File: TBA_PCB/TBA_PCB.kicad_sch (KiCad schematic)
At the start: 0 parts

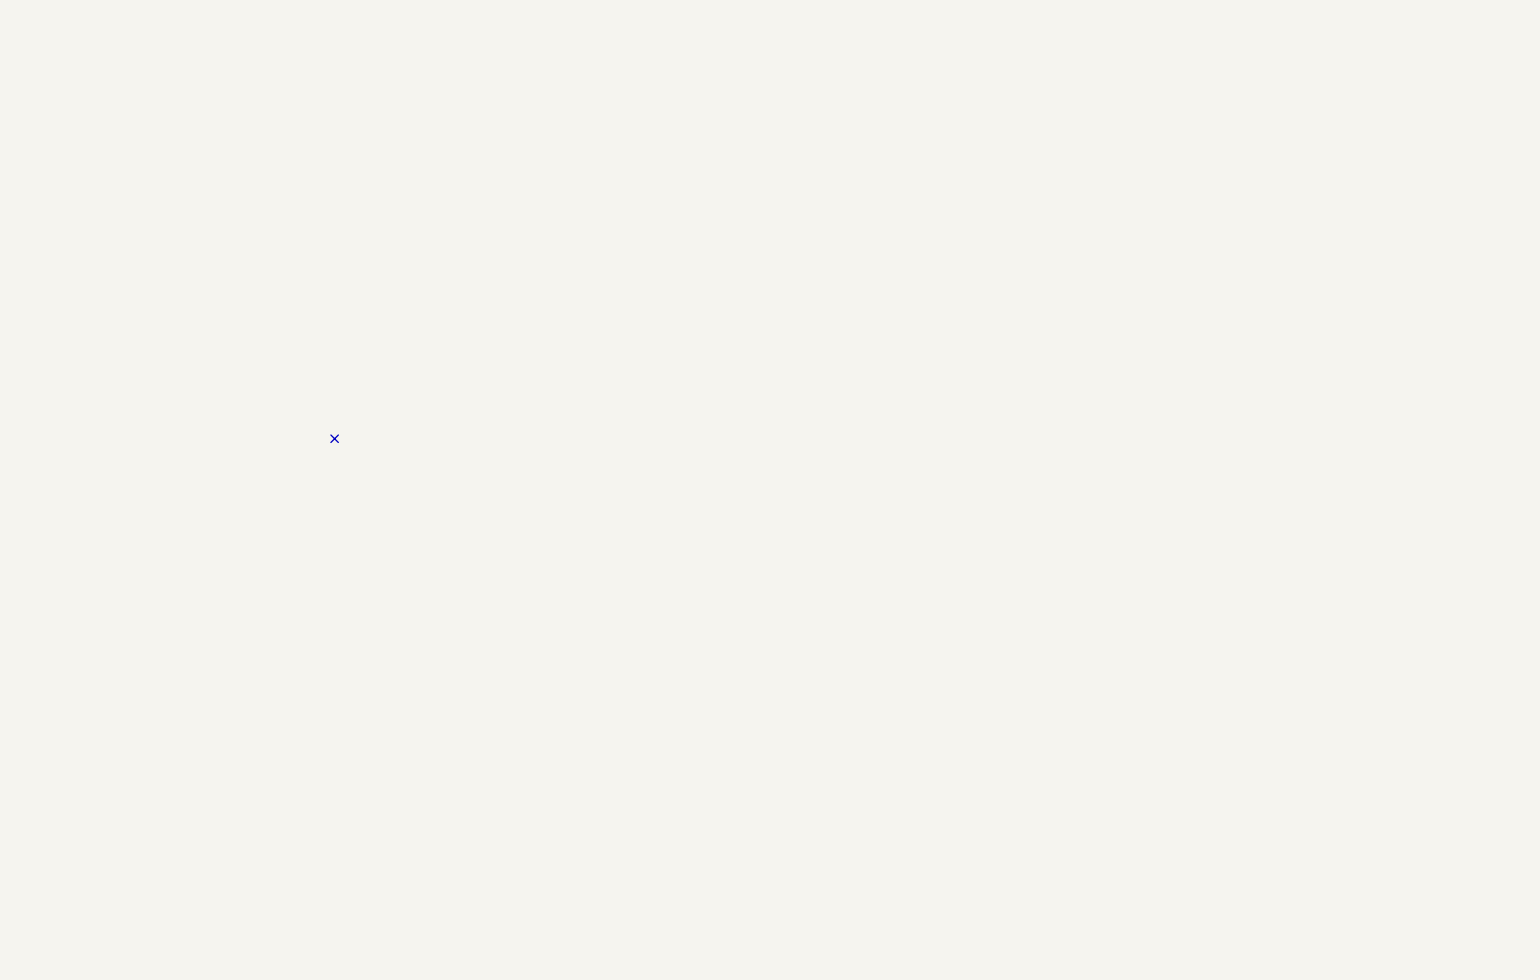
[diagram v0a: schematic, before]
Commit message: included practice threshold, updated PCB, gathered new data to plot
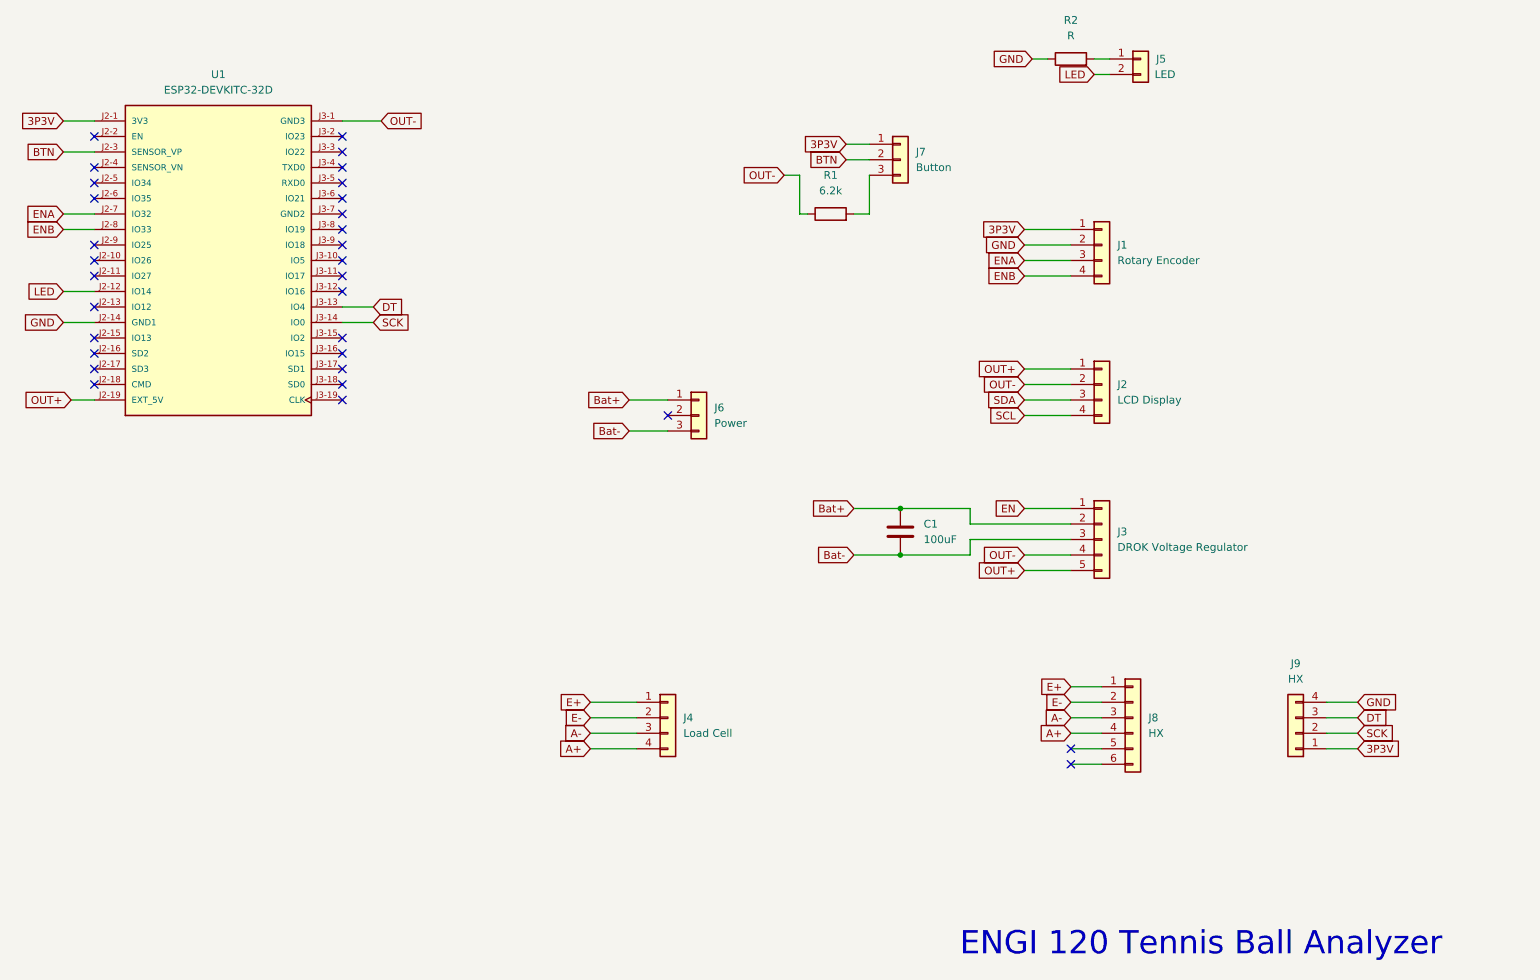
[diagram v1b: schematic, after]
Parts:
- added C1: 100uF, Capacitor_THT:CP_Radial_D4.0mm_P2.00mm, symbol Device:C
- added J1: Rotary Encoder, Connector_PinHeader_2.54mm:PinHeader_1x04_P2.54mm_Vertical, symbol Connector_Generic:Conn_01x04
- added J2: LCD Display, Connector_PinHeader_2.54mm:PinHeader_1x04_P2.54mm_Vertical, symbol Connector_Generic:Conn_01x04
- added J3: DROK Voltage Regulator, Connector_PinHeader_2.54mm:PinHeader_1x05_P2.54mm_Vertical, symbol Connector_Generic:Conn_01x05
- added J4: Load Cell, Connector_PinHeader_2.54mm:PinHeader_1x04_P2.54mm_Vertical, symbol Connector_Generic:Conn_01x04
- added J5: LED, Connector_PinHeader_2.54mm:PinHeader_1x02_P2.54mm_Vertical, symbol Connector_Generic:Conn_01x02
- added J6: Power, Connector_PinHeader_2.54mm:PinHeader_1x03_P2.54mm_Vertical, symbol Connector_Generic:Conn_01x03
- added J7: Button, Connector_PinHeader_2.54mm:PinHeader_1x03_P2.54mm_Vertical, symbol Connector_Generic:Conn_01x03
- added J8: HX, Connector_PinHeader_2.54mm:PinHeader_1x06_P2.54mm_Vertical, symbol Connector_Generic:Conn_01x06
- added J9: HX, Connector_PinHeader_2.54mm:PinHeader_1x04_P2.54mm_Vertical, symbol Connector_Generic:Conn_01x04
- added R1: 6.2k, Resistor_THT:R_Axial_DIN0204_L3.6mm_D1.6mm_P2.54mm_Vertical, symbol Device:R
- added R2: R, Resistor_THT:R_Axial_DIN0204_L3.6mm_D1.6mm_P2.54mm_Vertical, symbol Device:R
- added U1: ESP32-DEVKITC-32D, KiCad Footprints:MODULE_ESP32-DEVKITC-32D, symbol ESP32-DEVKITC-32D:ESP32-DEVKITC-32D
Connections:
- new net: J7.3 (Pin_3), R1.2
- new net: J5.1 (Pin_1), R2.2
- new net 3P3V: J1.1 (Pin_1), J7.1 (Pin_1), J9.1 (Pin_1), U1.J2-1 (3V3)
- new net A+: J4.4 (Pin_4), J8.4 (Pin_4)
- new net A-: J4.3 (Pin_3), J8.3 (Pin_3)
- new net BTN: J7.2 (Pin_2), U1.J2-3 (SENSOR_VP)
- new net Bat+: C1.1, J3.2 (Pin_2), J6.1 (Pin_1)
- new net Bat-: C1.2, J3.3 (Pin_3), J6.3 (Pin_3)
- new net DT: J9.3 (Pin_3), U1.J3-13 (IO4)
- new net E+: J4.1 (Pin_1), J8.1 (Pin_1)
- new net E-: J4.2 (Pin_2), J8.2 (Pin_2)
- new net EN: J3.1 (Pin_1)
- new net ENA: J1.3 (Pin_3), U1.J2-7 (IO32)
- new net ENB: J1.4 (Pin_4), U1.J2-8 (IO33)
- new net GND: J1.2 (Pin_2), J9.4 (Pin_4), R2.1, U1.J2-14 (GND1)
- new net LED: J5.2 (Pin_2), U1.J2-12 (IO14)
- new net OUT+: J2.1 (Pin_1), J3.5 (Pin_5), U1.J2-19 (EXT_5V)
- new net OUT-: J2.2 (Pin_2), J3.4 (Pin_4), R1.1, U1.J3-1 (GND3)
- new net SCK: J9.2 (Pin_2), U1.J3-14 (IO0)
- new net SCL: J2.4 (Pin_4)
- new net SDA: J2.3 (Pin_3)
- no-connect marks 1 -> 31
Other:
- note added: "ENGI 120 Tennis Ball Analyzer"
